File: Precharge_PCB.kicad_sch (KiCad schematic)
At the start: 71 parts, among them J1 MolexMicrofitPlus, J2 MolexMicrofitPlus, J3 MolexMicrofitPlus, J4 Conn_01x08, J5 SWD, J8 MolexMicrofitPlus, K1 G2RL-1A, K5 G2RL-1A, Q4 DMN61D8LQ, Q5 DMN61D8LQ, SW1 SW_Push, U1 SN65HVD1050D, U3 TPS7B88, U4 STM32F103C8Tx, U5 MCP1700x-330xxMB, Y1 8M

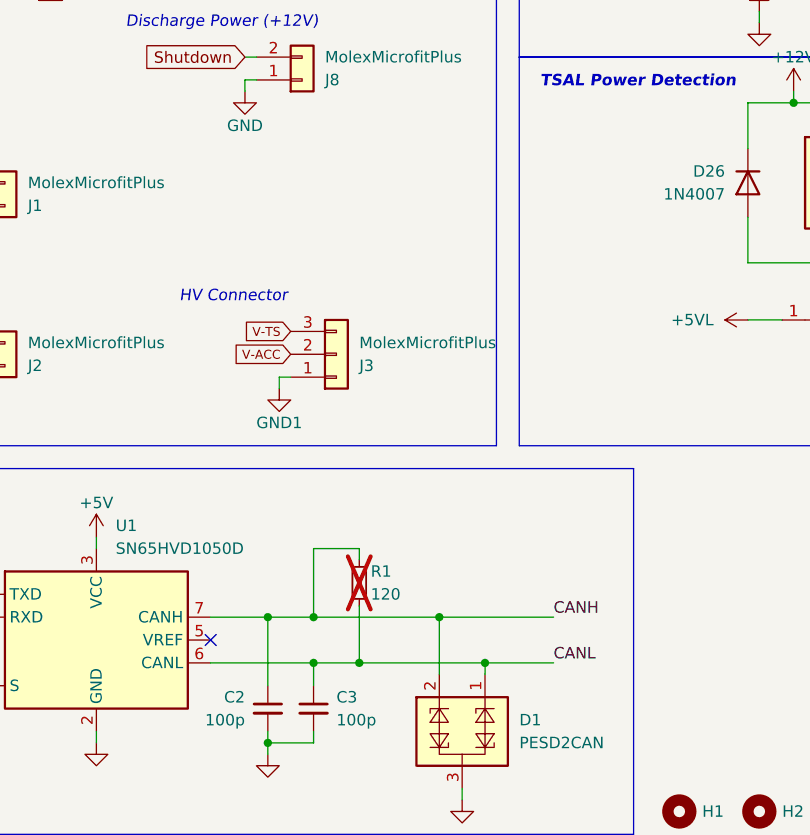
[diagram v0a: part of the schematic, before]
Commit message: schematic: Add a CAN connector
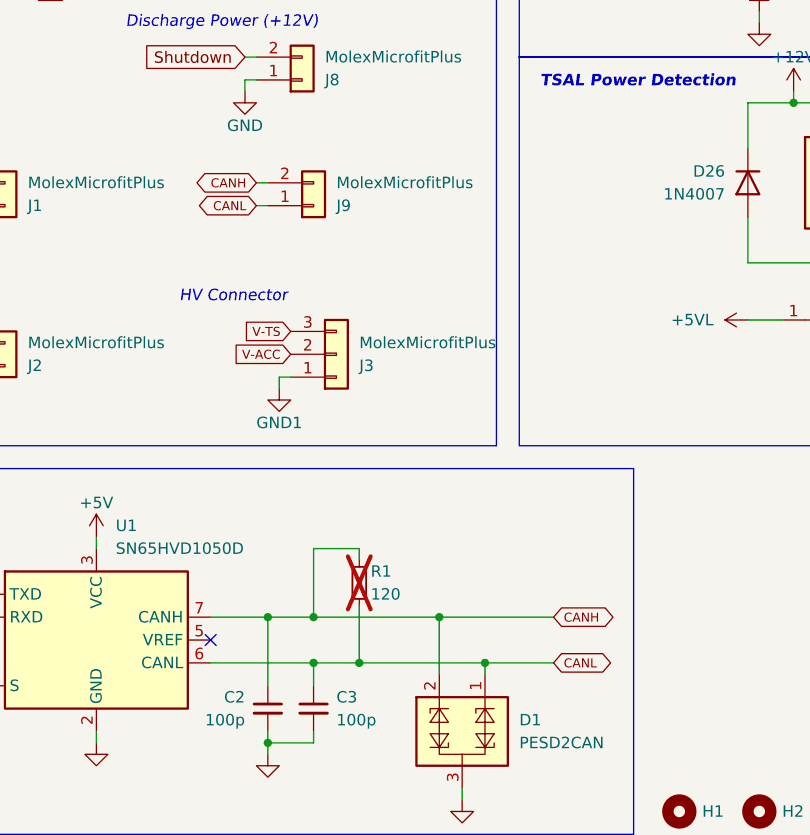
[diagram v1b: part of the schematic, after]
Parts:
- added J9: MolexMicrofitPlus, MyLibrary:MolexMicrofitPlus1x2, symbol Connector_Generic:Conn_01x02
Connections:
- net CANH: now also J9.2 (Pin_2)
- net CANL: now also J9.1 (Pin_1)
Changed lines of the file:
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@@
 	(wire
 		(pts
+			(xy 62.23 125.73) (xy 63.5 125.73)
+		)
+		(stroke
+			(width 0)
+			(type default)
+		)
+	)
+	(wire
+		(pts
 			(xy 186.69 140.97) (xy 191.77 140.97)
 		)
@@
 	(wire
 		(pts
+			(xy 63.5 123.19) (xy 62.23 123.19)
+		)
+		(stroke
+			(width 0)
+			(type default)
+		)
+	)
+	(wire
+		(pts
 			(xy 138.43 142.24) (xy 147.32 142.24)
 		)
@@
 		)
 	)
-	(label "CANL"
-		(at 95.25 176.53 0)
-		(effects
-			(font
-				(size 1.27 1.27)
-			)
-			(justify left bottom)
-		)
-	)
 	(label "Precharge-_ACT"
 		(at 138.43 27.94 0)
@@
 		)
 	)
-	(label "CANH"
-		(at 95.25 171.45 0)
-		(effects
-			(font
-				(size 1.27 1.27)
-			)
-			(justify left bottom)
-		)
-	)
 	(label "AIR-_CMD"
 		(at 30.48 58.42 180)
@@
 		)
 	)
+	(global_label "CANL"
+		(shape bidirectional)
+		(at 95.25 176.53 0)
+		(fields_autoplaced yes)
+		(effects
+			(font
+				(size 1 1)
+			)
+			(justify left)
+		)
+		(property "Intersheetrefs" "${INTERSHEET_REFS}"
+			(at 102.1895 176.53 0)
+			(effects
+				(font
+					(size 1.27 1.27)
+				)
+				(justify left)
+				(hide yes)
+			)
+		)
+	)
 	(global_label "CAN_TX"
 		(shape output)
@@
 		)
 	)
+	(global_label "CANH"
+		(shape bidirectional)
+		(at 62.23 123.19 180)
+		(fields_autoplaced yes)
+		(effects
+			(font
+				(size 1 1)
+			)
+			(justify right)
+		)
+		(property "Intersheetrefs" "${INTERSHEET_REFS}"
+			(at 55.0524 123.19 0)
+			(effects
+				(font
+					(size 1.27 1.27)
+				)
+				(justify right)
+				(hide yes)
+			)
+		)
+	)
 	(global_label "MCU_SHUTDOWN"
 		(shape input)
@@
 		)
 	)
+	(global_label "CANH"
+		(shape bidirectional)
+		(at 95.25 171.45 0)
+		(fields_autoplaced yes)
+		(effects
+			(font
+				(size 1 1)
+			)
+			(justify left)
+		)
+		(property "Intersheetrefs" "${INTERSHEET_REFS}"
+			(at 102.4276 171.45 0)
+			(effects
+				(font
+					(size 1.27 1.27)
+				)
+				(justify left)
+				(hide yes)
+			)
+		)
+	)
 	(global_label "Shutdown In"
 		(shape input)
@@
 		)
 	)
+	(global_label "CANL"
+		(shape bidirectional)
+		(at 62.23 125.73 180)
+		(fields_autoplaced yes)
+		(effects
+			(font
+				(size 1 1)
+			)
+			(justify right)
+		)
+		(property "Intersheetrefs" "${INTERSHEET_REFS}"
+			(at 55.2905 125.73 0)
+			(effects
+				(font
+					(size 1.27 1.27)
+				)
+				(justify right)
+				(hide yes)
+			)
+		)
+	)
 	(global_label "Shutdown In"
 		(shape input)
@@
 					(unit 1)
 				)
+			)
+		)
+	)
+	(symbol
+		(lib_id "Connector_Generic:Conn_01x02")
+		(at 68.58 125.73 0)
+		(mirror x)
+		(unit 1)
+		(exclude_from_sim no)
+		(in_bom yes)
+		(on_board yes)
+		(dnp no)
+		(property "Reference" "J9"
+			(at 71.12 125.7301 0)
+			(effects
+				(font
+					(size 1.27 1.27)
+				)
+				(justify left)
+			)
+		)
+		(property "Value" "MolexMicrofitPlus"
+			(at 71.12 123.1901 0)
+			(effects
+				(font
+					(size 1.27 1.27)
+				)
+				(justify left)
+			)
+		)
+		(property "Footprint" "MyLibrary:MolexMicrofitPlus1x2"
+			(at 68.58 125.73 0)
+			(effects
+				(font
+					(size 1.27 1.27)
+				)
+				(hide yes)
+			)
+		)
+		(property "Datasheet" "~"
+			(at 68.58 125.73 0)
+			(effects
+				(font
+					(size 1.27 1.27)
+				)
+				(hide yes)
+			)
+		)
+		(property "Description" "Generic connector, single row, 01x02, script generated (kicad-library-utils/schlib/autogen/connector/)"
+			(at 68.58 125.73 0)
+			(effects
+				(font
+					(size 1.27 1.27)
+				)
+				(hide yes)
+			)
+		)
+		(pin "1"
+		)
+		(pin "2"
+		)
+		(instances
+			(project "Precharge_PCB"
+				(path "/c467677d-b98c-4488-bd11-965ef67263b2"
+					(reference "J9")
+					(unit 1)
+				)

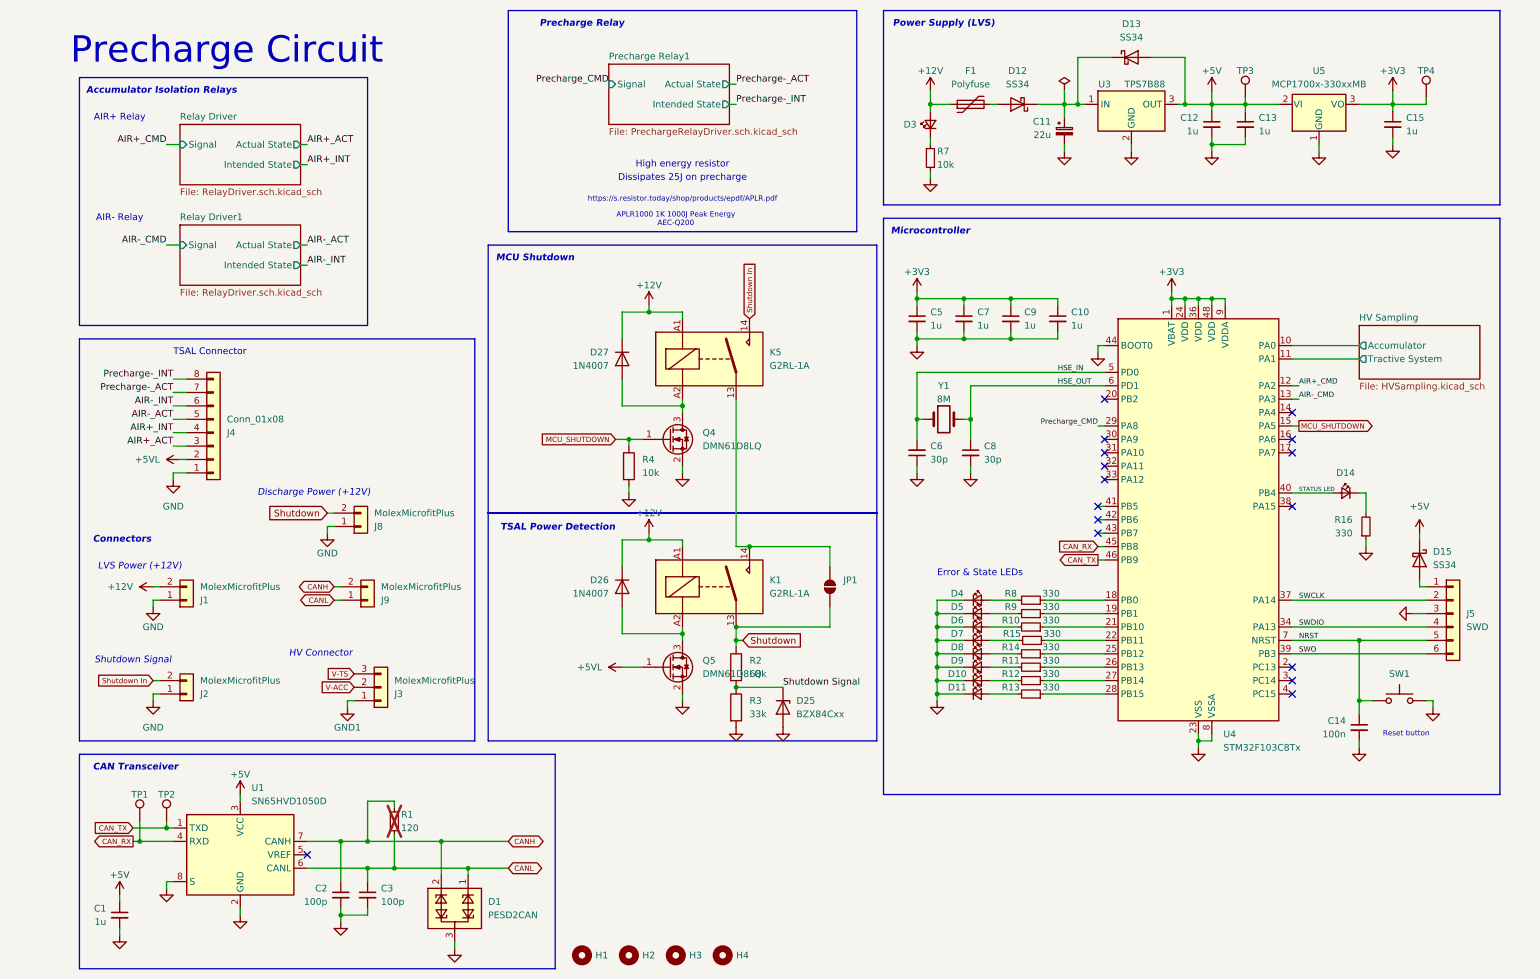
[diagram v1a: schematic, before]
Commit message: Updated to single pole relay, removed relay drivers
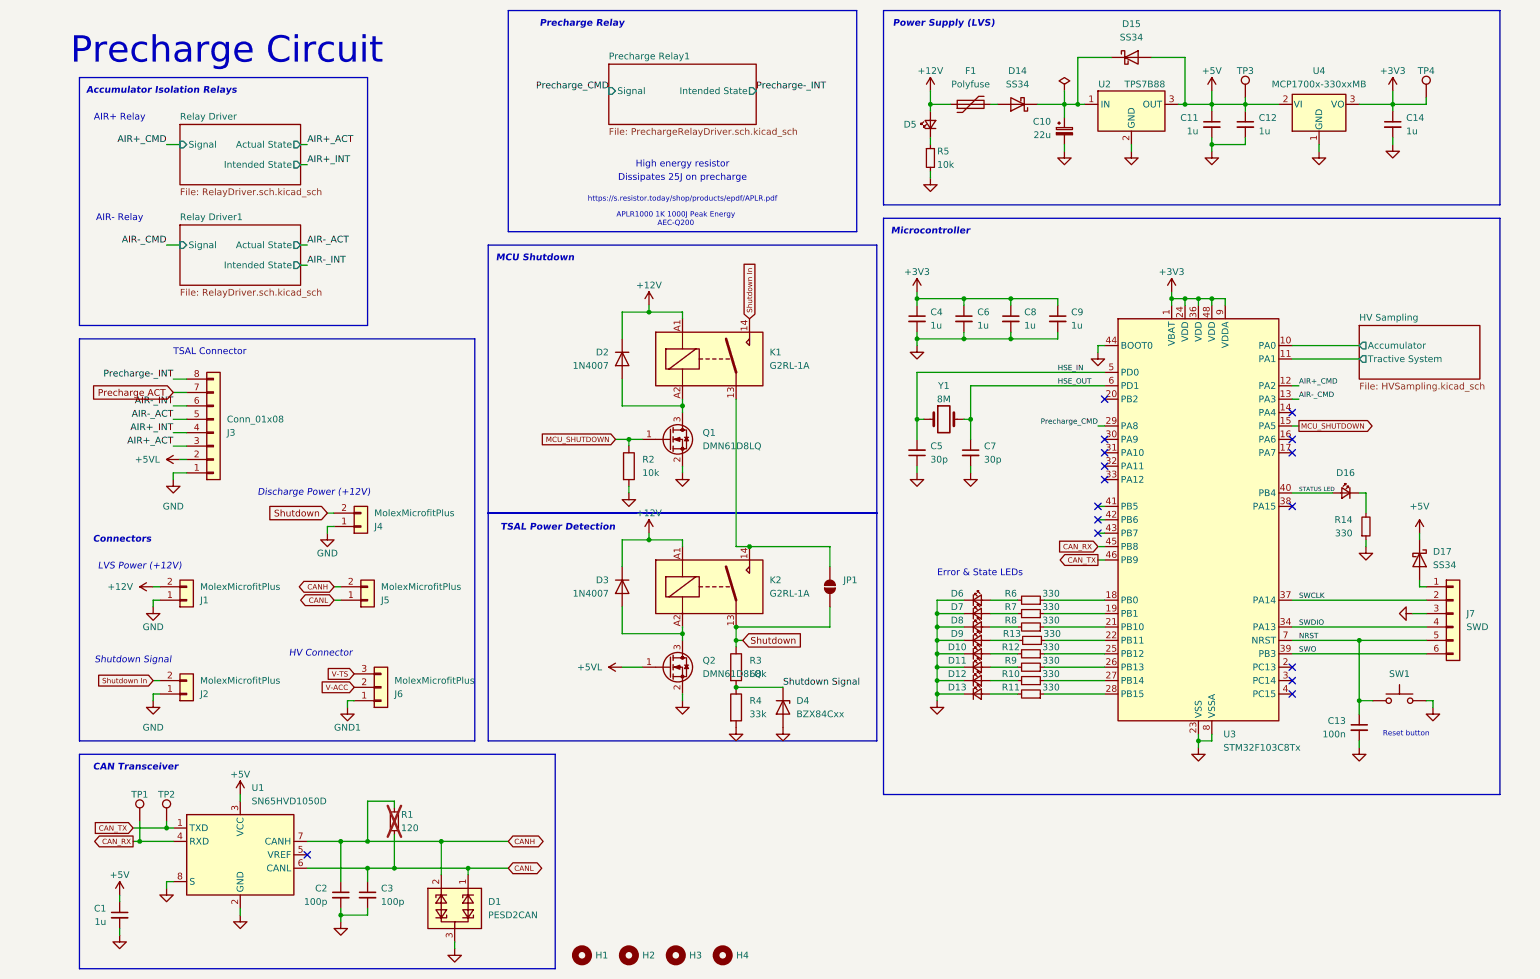
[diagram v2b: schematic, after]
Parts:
- R2: renamed from R4; footprint (none) -> Resistor_SMD:R_0603_1608Metric
- R3: renamed from R2; footprint (none) -> Resistor_SMD:R_0603_1608Metric
- R4: renamed from R3; footprint (none) -> Resistor_SMD:R_0603_1608Metric
- renumbered C11 to C10, C12 to C11, C13 to C12, C14 to C13, C15 to C14, C5 to C4, C6 to C5, C7 to C6, C8 to C7, C9 to C8, C10 to C9, D8 to D10, D9 to D11, D10 to D12, D11 to D13, D12 to D14, D13 to D15, D14 to D16, D15 to D17, D27 to D2, D26 to D3, D25 to D4, D3 to D5, D4 to D6, D5 to D7, D6 to D8, D7 to D9, J4 to J3, J8 to J4, J9 to J5, J3 to J6, J5 to J7, K5 to K1, K1 to K2, Q4 to Q1, Q5 to Q2, R12 to R10, R13 to R11, R14 to R12, R15 to R13, R16 to R14, R7 to R5, R8 to R6, R9 to R7, R10 to R8, R11 to R9, U3 to U2, U4 to U3, U5 to U4
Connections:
- net Precharge-_ACT renamed Precharge ACT
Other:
- sheet Precharge Relay1 ports: added none; removed Actual State

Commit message: schematic: Switch to NSR0530H from SS34
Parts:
- removed D14, D15, D17: SS34, Diode_SMD:D_SMA, symbol Diode:SS34
- added D14, D15, D22: D_Schottky, Diode_SMD:D_SOD-323, symbol Device:D_Schottky
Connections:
- net +5V: now also D14.2 (A), D15.1 (K)
- net at C10.1, U2.1 (IN): now also D14.1 (K), D22.1 (K)
- net at J7.1 (Pin_1): now also D15.2 (A)
- net at F1.2: now also D22.2 (A)

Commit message: schematic: Switch to new push button
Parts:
- removed SW1: SW_Push, Button_Switch_SMD:SW_Push_SPST_NO_Alps_SKRK, symbol Switch:SW_Push
- added SW2: SW_Push, Button_Switch_SMD:SW_Push_1P1T_NO_Vertical_Wuerth_434133025816, symbol Switch:SW_Push
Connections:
- net GND: now also SW2.2
- net NRST: now also SW2.1
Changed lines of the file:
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@@
+	)
+	(symbol
+		(lib_id "Switch:SW_Push")
+		(at 264.16 144.78 0)
+		(unit 1)
+		(exclude_from_sim no)
+		(in_bom yes)
+		(on_board yes)
+		(dnp no)
+		(property "Reference" "SW2"
+			(at 264.16 139.7 0)
+			(effects
+				(font
+					(size 1.27 1.27)
+				)
+			)
+		)
+		(property "Value" "SW_Push"
+			(at 264.16 139.7 0)
+			(effects
+				(font
+					(size 1.27 1.27)
+				)
+				(hide yes)
+			)
+		)
+		(property "Footprint" "Button_Switch_SMD:SW_Push_1P1T_NO_Vertical_Wuerth_434133025816"
+			(at 264.16 139.7 0)
+			(effects
+				(font
+					(size 1.27 1.27)
+				)
+				(hide yes)
+			)
+		)
+		(property "Datasheet" "~"
+			(at 264.16 139.7 0)
+			(effects
+				(font
+					(size 1.27 1.27)
+				)
+				(hide yes)
+			)
+		)
+		(property "Description" "Push button switch, generic, two pins"
+			(at 264.16 144.78 0)
+			(effects
+				(font
+					(size 1.27 1.27)
+				)
+				(hide yes)
+			)
+		)
+		(property "Dist #" "C139797"
+			(at 264.16 144.78 0)
+			(effects
+				(font
+					(size 1.27 1.27)
+				)
+				(hide yes)
+			)
+		)
+		(property "Mfr" "ALPSALPINE"
+			(at 264.16 144.78 0)
+			(effects
+				(font
+					(size 1.27 1.27)
+				)
+				(hide yes)
+			)
+		)
+		(property "Mfr #" "SKRPACE010"
+			(at 264.16 144.78 0)
+			(effects
+				(font
+					(size 1.27 1.27)
+				)
+				(hide yes)
+			)
+		)
+		(property "Dist" "LCSC"
+			(at 264.16 144.78 0)
+			(effects
+				(font
+					(size 1.27 1.27)
+				)
+				(hide yes)
+			)
+		)
+		(pin "2"
+		)
+		(pin "1"
+		)
+		(instances
+			(project "Precharge_PCB"
+				(path "/c467677d-b98c-4488-bd11-965ef67263b2"
+					(reference "SW2")
+					(unit 1)
+				)
+			)
+		)
 	)
 	(symbol
@@
 					(unit 1)
 				)
-			)
-		)
-	)
-	(symbol
-		(lib_id "Switch:SW_Push")
-		(at 264.16 144.78 0)
-		(unit 1)
-		(exclude_from_sim no)
-		(in_bom yes)
-		(on_board yes)
-		(dnp no)
-		(property "Reference" "SW1"
-			(at 264.16 139.7 0)
-			(effects
-				(font
-					(size 1.27 1.27)
-				)
-			)
-		)
-		(property "Value" "SW_Push"
-			(at 264.16 139.7 0)
-			(effects
-				(font
-					(size 1.27 1.27)
-				)
-				(hide yes)
-			)
-		)
-		(property "Footprint" "Button_Switch_SMD:SW_Push_SPST_NO_Alps_SKRK"
-			(at 264.16 139.7 0)
-			(effects
-				(font
-					(size 1.27 1.27)
-				)
-				(hide yes)
-			)
-		)
-		(property "Datasheet" "~"
-			(at 264.16 139.7 0)
-			(effects
-				(font
-					(size 1.27 1.27)
-				)
-				(hide yes)
-			)
-		)
-		(property "Description" "Push button switch, generic, two pins"
-			(at 264.16 144.78 0)
-			(effects
-				(font
-					(size 1.27 1.27)
-				)
-				(hide yes)
-			)
-		)
-		(property "Dist #" "C720477"
-			(at 264.16 144.78 0)
-			(effects
-				(font
-					(size 1.27 1.27)
-				)
-				(hide yes)
-			)
-		)
-		(property "Mfr" "XUNPU"
-			(at 264.16 144.78 0)
-			(effects
-				(font
-					(size 1.27 1.27)
-				)
-				(hide yes)
-			)
-		)
-		(property "Mfr #" "TS-1088-AR02016"
-			(at 264.16 144.78 0)
-			(effects
-				(font
-					(size 1.27 1.27)
-				)
-				(hide yes)
-			)
-		)
-		(property "Dist" "LCSC"
-			(at 264.16 144.78 0)
-			(effects
-				(font
-					(size 1.27 1.27)
-				)
-				(hide yes)
-			)
-		)
-		(pin "2"
-		)
-		(pin "1"
-		)
-		(instances
-			(project "Precharge_PCB"
-				(path "/c467677d-b98c-4488-bd11-965ef67263b2"
-					(reference "SW1")
-					(unit 1)
-				)

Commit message: schematic: Switch to new IDC SWD header
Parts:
- removed J7: SWD, Connector_PinHeader_2.54mm:PinHeader_1x06_P2.54mm_Vertical, symbol Connector_Generic:Conn_01x06
- added J10: Conn_01x06, yfs:IDC-Connector-2x3, symbol Connector_Generic:Conn_01x06
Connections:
- net GND: now also J10.3 (Pin_3)
- net NRST: now also J10.5 (Pin_5)
- net SWCLK: now also J10.2 (Pin_2)
- net SWDIO: now also J10.4 (Pin_4)
- net SWO: now also J10.6 (Pin_6)
- net at D15.2 (A): now also J10.1 (Pin_1)
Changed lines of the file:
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@@
-	)
-	(symbol
-		(lib_id "Connector_Generic:Conn_01x06")
-		(at 274.32 128.27 0)
-		(unit 1)
-		(exclude_from_sim no)
-		(in_bom yes)
-		(on_board yes)
-		(dnp no)
-		(fields_autoplaced yes)
-		(property "Reference" "J7"
-			(at 276.86 128.2699 0)
-			(effects
-				(font
-					(size 1.27 1.27)
-				)
-				(justify left)
-			)
-		)
-		(property "Value" "SWD"
-			(at 276.86 130.8099 0)
-			(effects
-				(font
-					(size 1.27 1.27)
-				)
-				(justify left)
-			)
-		)
-		(property "Footprint" "Connector_PinHeader_2.54mm:PinHeader_1x06_P2.54mm_Vertical"
-			(at 274.32 128.27 0)
-			(effects
-				(font
-					(size 1.27 1.27)
-				)
-				(hide yes)
-			)
-		)
-		(property "Datasheet" "~"
-			(at 274.32 128.27 0)
-			(effects
-				(font
-					(size 1.27 1.27)
-				)
-				(hide yes)
-			)
-		)
-		(property "Description" "Generic connector, single row, 01x06, script generated (kicad-library-utils/schlib/autogen/connector/)"
-			(at 274.32 128.27 0)
-			(effects
-				(font
-					(size 1.27 1.27)
-				)
-				(hide yes)
-			)
-		)
-		(property "Dist #" "C6332200"
-			(at 274.32 128.27 0)
-			(effects
-				(font
-					(size 1.27 1.27)
-				)
-				(hide yes)
-			)
-		)
-		(property "Mfr" "Hanbo Electronic"
-			(at 274.32 128.27 0)
-			(effects
-				(font
-					(size 1.27 1.27)
-				)
-				(hide yes)
-			)
-		)
-		(property "Mfr #" "HB-PH3-25417PB2GOP"
-			(at 274.32 128.27 0)
-			(effects
-				(font
-					(size 1.27 1.27)
-				)
-				(hide yes)
-			)
-		)
-		(property "Dist" "LCSC"
-			(at 274.32 128.27 0)
-			(effects
-				(font
-					(size 1.27 1.27)
-				)
-				(hide yes)
-			)
-		)
-		(pin "5"
-		)
-		(pin "1"
-		)
-		(pin "4"
-		)
-		(pin "3"
-		)
-		(pin "2"
-		)
-		(pin "6"
-		)
-		(instances
-			(project "Precharge_PCB"
-				(path "/c467677d-b98c-4488-bd11-965ef67263b2"
-					(reference "J7")
-					(unit 1)
-				)
-			)
-		)
 	)
 	(symbol
@@
 					(unit 1)
 				)
+			)
+		)
+	)
+	(symbol
+		(lib_id "Connector_Generic:Conn_01x06")
+		(at 274.32 128.27 0)
+		(unit 1)
+		(exclude_from_sim no)
+		(in_bom yes)
+		(on_board yes)
+		(dnp no)
+		(property "Reference" "J10"
+			(at 273.05 138.43 0)
+			(effects
+				(font
+					(size 1.27 1.27)
+				)
+				(justify left)
+			)
+		)
+		(property "Value" "Conn_01x06"
+			(at 276.86 130.8099 0)
+			(effects
+				(font
+					(size 1.27 1.27)
+				)
+				(justify left)
+				(hide yes)
+			)
+		)
+		(property "Footprint" "yfs:IDC-Connector-2x3"
+			(at 274.32 128.27 0)
+			(effects
+				(font
+					(size 1.27 1.27)
+				)
+				(hide yes)
+			)
+		)
+		(property "Datasheet" "~"
+			(at 274.32 128.27 0)
+			(effects
+				(font
+					(size 1.27 1.27)
+				)
+				(hide yes)
+			)
+		)
+		(property "Description" "Generic connector, single row, 01x06, script generated (kicad-library-utils/schlib/autogen/connector/)"
+			(at 274.32 128.27 0)
+			(effects
+				(font
+					(size 1.27 1.27)
+				)
+				(hide yes)
+			)
+		)
+		(property "Dist #" "C42372545"
+			(at 274.32 128.27 0)
+			(effects
+				(font
+					(size 1.27 1.27)
+				)
+				(hide yes)
+			)
+		)
+		(property "Mfr" "hanxia"
+			(at 274.32 128.27 0)
+			(effects
+				(font
+					(size 1.27 1.27)
+				)
+				(hide yes)
+			)
+		)
+		(property "Mfr #" "HX JN1.27-2x3P ZZ H4.9"
+			(at 274.32 128.27 0)
+			(effects
+				(font
+					(size 1.27 1.27)
+				)
+				(hide yes)
+			)
+		)
+		(property "Dist" "LCSC"
+			(at 274.32 128.27 0)
+			(effects
+				(font
+					(size 1.27 1.27)
+				)
+				(hide yes)
+			)
+		)
+		(pin "5"
+		)
+		(pin "1"
+		)
+		(pin "4"
+		)
+		(pin "3"
+		)
+		(pin "2"
+		)
+		(pin "6"
+		)
+		(instances
+			(project "Precharge_PCB"
+				(path "/c467677d-b98c-4488-bd11-965ef67263b2"
+					(reference "J10")
+					(unit 1)
+				)
